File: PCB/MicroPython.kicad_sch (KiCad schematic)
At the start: 64 parts, among them J1 Conn_01x08, J10 USB4105-GF-A, J11 Micro_SD_Card, J3 Conn_01x08, J4 Conn_01x08, J5 Conn_02x04_Odd_Even, J8 Conn_02x03_Odd_Even, J9 Conn_01x08, SW1 SW_SPST, SW2 SW_SPST, U1 STM32F405RGT6, U2 MCP1700T, U4 FXLS8971CFR1, X1 12 MHz, X2 32.768 kHz

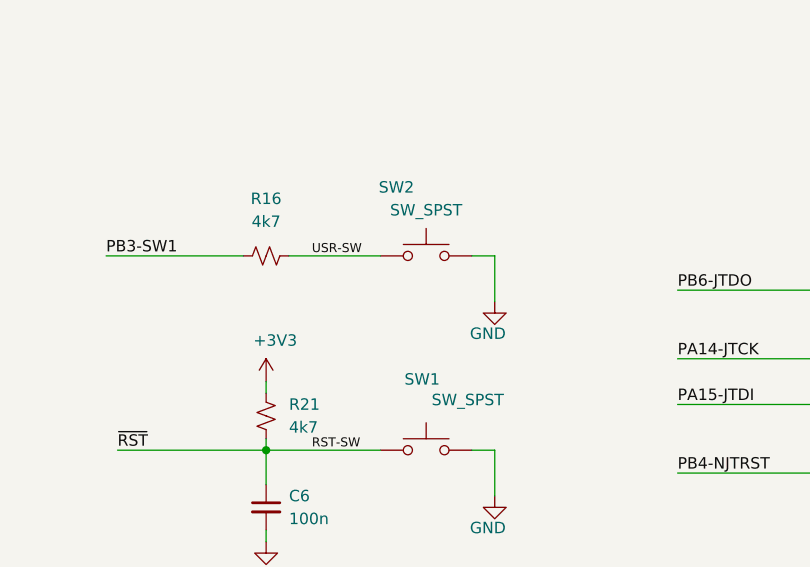
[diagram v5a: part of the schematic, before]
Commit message: mudanças a partir de mudanças sugeridas pelo Filipe
- projecto commited já com pequenas alterações do Filipe
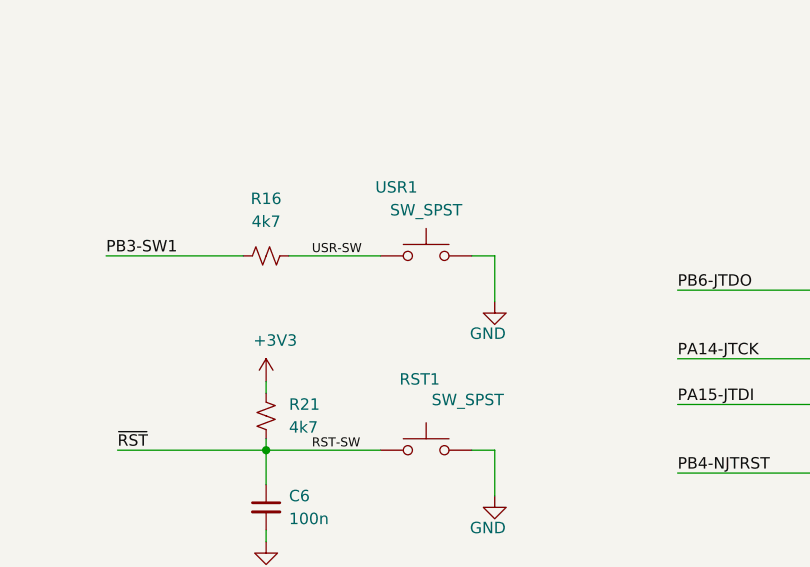
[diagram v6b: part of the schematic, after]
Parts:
- renumbered SW1 to RST1, SW2 to USR1
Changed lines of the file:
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@@
 		(on_board yes)
 		(dnp no)
-		(property "Reference" "SW1"
+		(property "Reference" "RST1"
 			(at 185.674 233.426 0)
 			(effects
@@
 			(project "PyBoard"
 				(path "/b5377262-2fbf-4f54-aca8-87c57de8d98e"
-					(reference "SW1")
+					(reference "RST1")
 					(unit 1)
 				)
@@
 		(on_board yes)
 		(dnp no)
-		(property "Reference" "SW2"
+		(property "Reference" "USR1"
 			(at 180.848 212.09 0)
 			(effects
@@
 			(project ""
 				(path "/b5377262-2fbf-4f54-aca8-87c57de8d98e"
-					(reference "SW2")
-					(unit 1)
-				)
+					(reference "USR1")
+					(unit 1)
+				)
